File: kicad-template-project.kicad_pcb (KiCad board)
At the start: 6 copper layers, 50 x 50 mm, 72 parts, among them J2 Conn_01x12, Q1 LMG2100R026, Q2 LMG2100R026, Q3 LMG2100R026, U1 MCS1823, U10 AD40xxBCPZ, U11 AD40xxBCPZ, U12 TPS54360DDA, U13 MIC5219YM5, U14 MIC5219YM5, U2 MCS1823, U3 MCS1823, U4 ICE40UP5K-SG48ITR, U5 STM32L432KBUx, U6 SN65HVD230, U7 MIC5219YM5, U8 MLX90395xLW, U9 AD40xxBCPZ

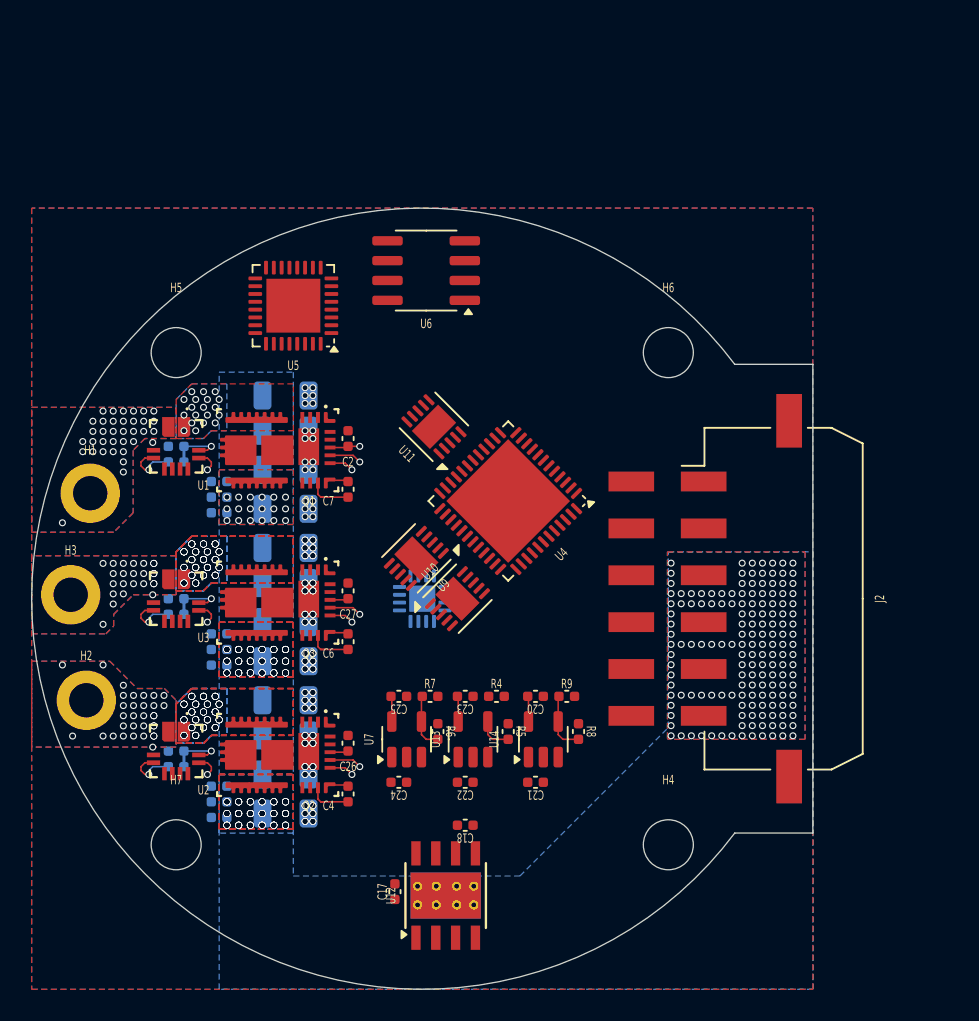
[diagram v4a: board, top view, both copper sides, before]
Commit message: fix: update fpga with power supply
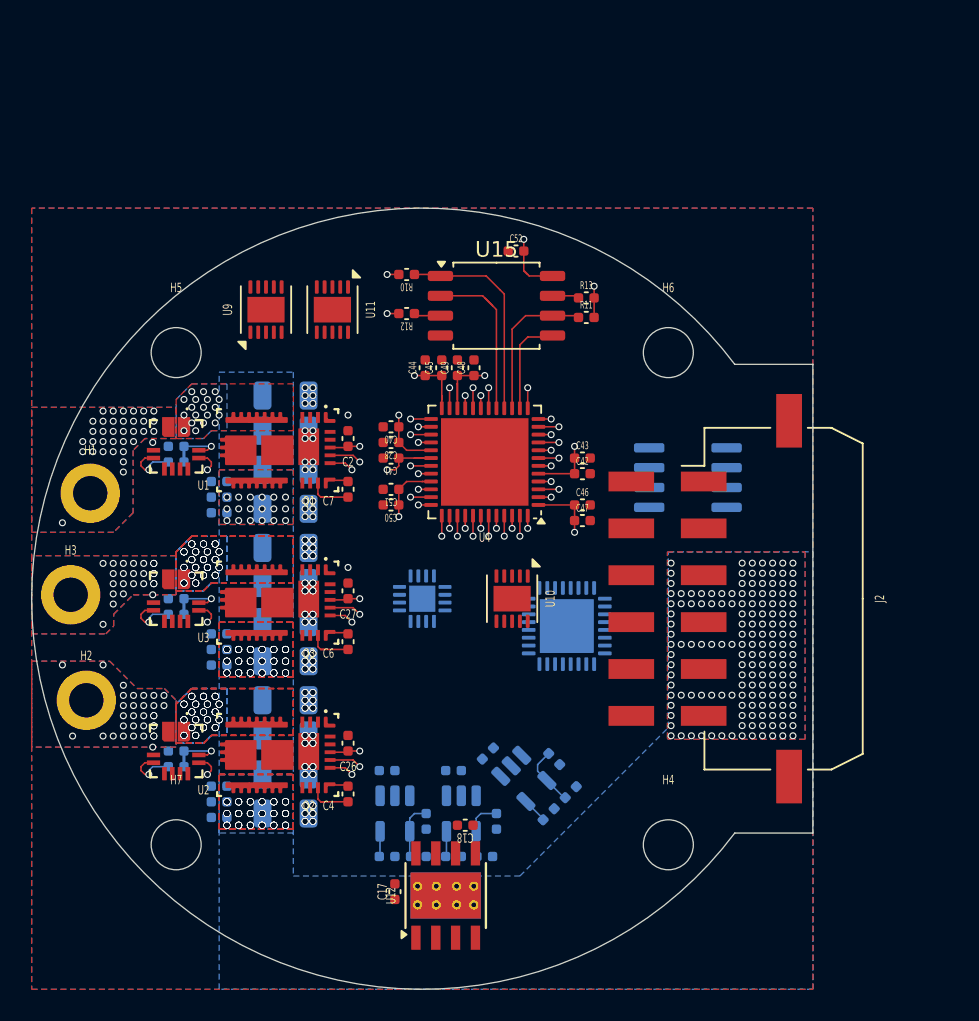
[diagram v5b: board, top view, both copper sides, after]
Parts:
- added C28: 100 nF, chenry-footprint-lib:C_0402, F.Cu at (128.0, 125.0)
- added C40: 4.7uF, chenry-footprint-lib:C_0402, F.Cu at (128.0, 124.0)
- added C41: 100 nF, chenry-footprint-lib:C_0402, F.Cu at (128.0, 126.0)
- added C42: 100 nF, chenry-footprint-lib:C_0402, F.Cu at (140.2, 127.0)
- added C43: 4.7uF, chenry-footprint-lib:C_0402, F.Cu at (140.2, 126.0)
- added C44: 4.7uF, chenry-footprint-lib:C_0402, F.Cu at (130.2, 120.2)
- added C45: 100 nF, chenry-footprint-lib:C_0402, F.Cu at (131.2, 120.2)
- added C46: 4.7uF, chenry-footprint-lib:C_0402, F.Cu at (140.2, 129.0)
- added C47: 100 nF, chenry-footprint-lib:C_0402, F.Cu at (140.2, 130.0)
- added C48: 4.7uF, chenry-footprint-lib:C_0402, F.Cu at (133.3, 120.2)
- added C49: 100 nF, chenry-footprint-lib:C_0402, F.Cu at (132.2, 120.2)
- added C50: 4.7uF, chenry-footprint-lib:C_0402, F.Cu at (128.0, 129.0)
- added C51: 100 nF, chenry-footprint-lib:C_0402, F.Cu at (128.0, 128.0)
- added C52: 100 nF, chenry-footprint-lib:C_0402, F.Cu at (136.0, 112.8)
- added R10: 10K, chenry-footprint-lib:R_0402, F.Cu at (129.0, 114.2)
- added R11: 10K, chenry-footprint-lib:R_0402, F.Cu at (140.5, 117.0)
- added R12: 10K, chenry-footprint-lib:R_0402, F.Cu at (129.0, 116.7)
- added R13: 10K, chenry-footprint-lib:R_0402, F.Cu at (140.5, 115.8)
- added U15: W25Q16JVSS, Package_SO:SOIC-8_5.3x5.3mm_P1.27mm, F.Cu at (134.8, 116.2)
- C20, C21, C22, C23, C24, C25, R4, R5, R6, R7, R8, R9, U13, U14, U5, U6, U7: moved to B.Cu
- moved U5 27.0 mm to (139.2, 136.8), turned to 0 degrees
- moved U6 21.4 mm to (147.0, 127.2)
- moved U9 18.6 mm to (120.0, 116.5), turned to 90 degrees
- moved C25 10.3 mm to (127.7, 151.5)
- moved R4 10.3 mm to (134.0, 151.5)
- moved R7 10.3 mm to (129.7, 151.5)
- moved C23 10.3 mm to (132.0, 151.5)
- moved U11 9.92 mm to (124.2, 116.5), turned to -90 degrees
- moved C20 7.59 mm to (138.1, 148.8), turned to -135 degrees
- moved R9 6.14 mm to (139.5, 147.4), turned to 45 degrees
- moved R6 5.80 mm to (130.2, 149.2), turned to 90 degrees
- moved R5 5.80 mm to (134.8, 149.2), turned to 90 degrees
- moved U13 4.81 mm to (132.5, 148.8), turned to -90 degrees
- moved U7 4.81 mm to (128.2, 148.8), turned to -90 degrees
- moved C21 3.56 mm to (134.2, 144.9), turned to -135 degrees
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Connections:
- net Net-(U4D-VCC-Pad30) renamed VDD_1V2
- U4 pad 1: unconnected-(U4C-VCCIO_2-Pad1) -> VDD_3V3
- U4 pad 14: unconnected-(U4B-IOB_32a_SPI_SO-Pad14) -> /FPGA/FLASH_MOSI
- U4 pad 15: unconnected-(U4B-IOB_34a_SPI_SCK-Pad15) -> /FPGA/FLASH_CLK
- U4 pad 16: unconnected-(U4B-IOB_35b_SPI_SS-Pad16) -> /FPGA/FLASH_CS
- U4 pad 17: unconnected-(U4B-IOB_33b_SPI_SI-Pad17) -> /FPGA/FLASH_MISO
- U4 pad 22: unconnected-(U4B-SPI_VCCIO1-Pad22) -> VDD_3V3
- U4 pad 24: unconnected-(U4D-VPP_2V5-Pad24) -> VDD_3V3
- U4 pad 29: unconnected-(U4D-VCCPLL-Pad29) -> VDD_3V3
- U4 pad 33: unconnected-(U4A-VCCIO_0-Pad33) -> VDD_3V3
- U4 pad 49: unconnected-(U4D-GND-Pad49) -> GND
- U8 pad 10: Net-(U8-V_{SS}-Pad10) -> GND
- U8 pad 13: Net-(U8-V_{SS}-Pad10) -> GND
- U8 pad 14: Net-(U8-V_{SS}-Pad10) -> GND
- U8 pad 15: unconnected-(U8-V_{DD}-Pad15) -> VDD_3V3
- U8 pad 16: Net-(U8-V_{SS}-Pad10) -> GND
- U8 pad 17: Net-(U8-V_{SS}-Pad10) -> GND
- U8 pad 4: Net-(U8-V_{SS}-Pad10) -> GND
- U8 pad 8: Net-(U8-V_{SS}-Pad10) -> GND
- U8 pad 9: Net-(U8-V_{SS}-Pad10) -> GND
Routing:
- net VDD_3V3: track 12.6 -> 41.6 mm, vias 3 -> 12
- net /FPGA/FLASH_CS: track 0.00 -> 13.5 mm
- net /FPGA/FLASH_MISO: track 0.00 -> 11.0 mm
- net /PH0/ISNS: track 3.52 -> 13.7 mm, vias 1 -> 2
- net /FPGA/FLASH_CLK: track 0.00 -> 9.72 mm
- net /PH2/ISNS: track 3.52 -> 12.7 mm, vias 1 -> 2
- net VDD_1V2: track 0.00 -> 8.04 mm, vias 0 -> 2
- net /FPGA/FLASH_MOSI: track 0.00 -> 6.52 mm
- net Net-(U15-~{WP}/IO_{2}): track 0.00 -> 1.72 mm
- net Net-(U15-~{HOLD}/~{RESET}/IO_{3}): track 0.00 -> 1.72 mm
- net VDD_5V: track 5.93 -> 7.43 mm, vias 1 -> 3
- net unconnected-(U4C-IOB_9b-Pad3): track 0.00 -> 1.31 mm, vias 0 -> 1
- net unconnected-(U4B-IOB_25b_G3-Pad20): track 0.00 -> 1.31 mm, vias 0 -> 1
- net unconnected-(U4A-RGB2-Pad41): track 0.00 -> 1.31 mm, vias 0 -> 1
- net unconnected-(U4A-RGB0-Pad39): track 0.00 -> 1.31 mm, vias 0 -> 1
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
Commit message: fix: added placeholder stlink connector
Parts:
- added J1: Conn_ST_STDC14, Connector_PinHeader_1.27mm:PinHeader_2x07_P1.27mm_Vertical_SMD, F.Cu at (137.0, 142.8)
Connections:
- U5 pad 23: unconnected-(U5-PA13-Pad23) -> /MCU/SWDIO
- U5 pad 24: unconnected-(U5-PA14-Pad24) -> /MCU/SWCLK
- U5 pad 4: unconnected-(U5-NRST-Pad4) -> /MCU/NRST
